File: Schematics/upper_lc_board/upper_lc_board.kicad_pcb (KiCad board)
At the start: 4 copper layers, 69.5 x 60 mm, 102 parts, among them J1 Stack Male Edge Connector, J3 PT, J4 TC, J5 SOL_CONN, J6 SOL2_CONN, Q1 MOSFET_BSS138, U1 ESP32-S3-WROOM-1-N16R2, U2 CAN_T_SN65HVD230DR, U3 PD_D3V3XA4B10LP, U4 ID_LM66100DCKR, U5 ID_LM66100DCKR, U6 TLV75801PDRV, U7 ADS131M04IPWR, U8 SSR_VO1400AEFTR, Y1 CRYSTAL_SIT8208AI

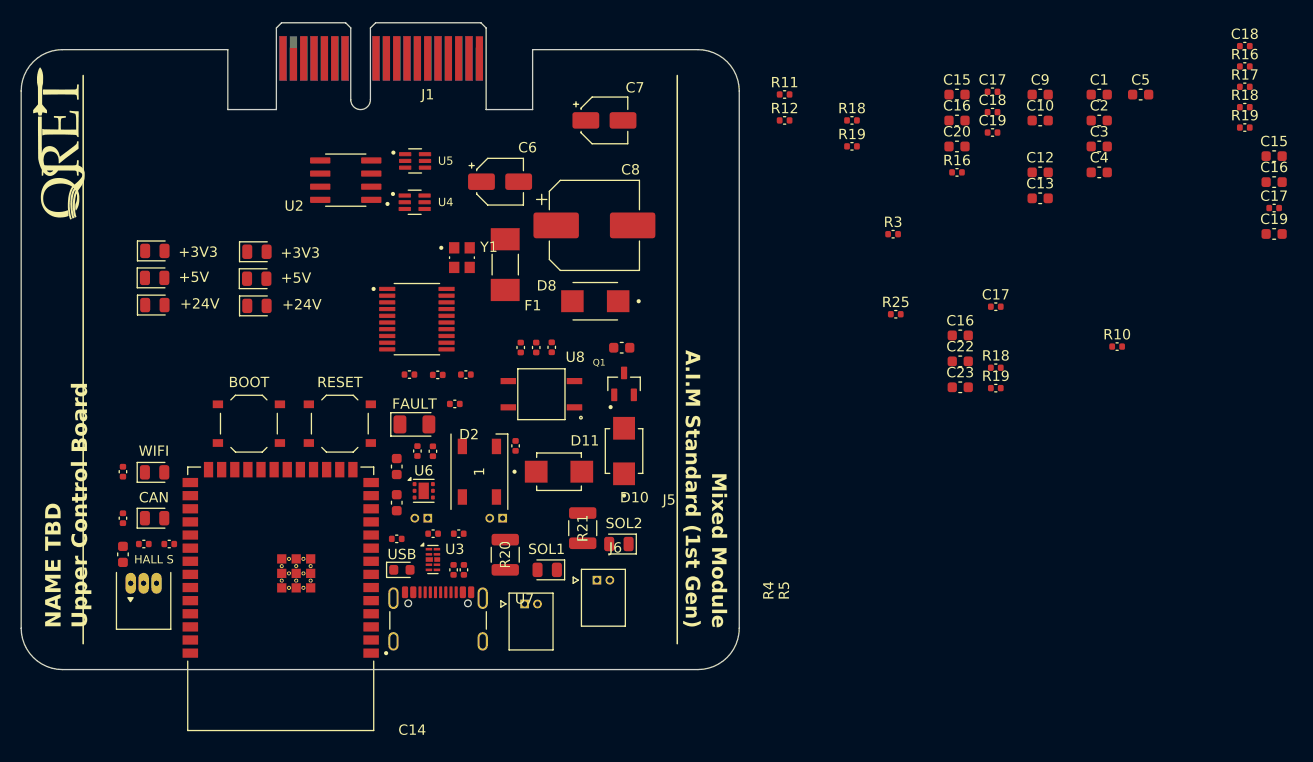
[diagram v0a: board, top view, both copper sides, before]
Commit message: update power circuitry (replaced OR-ing setup with a single power mux IC)
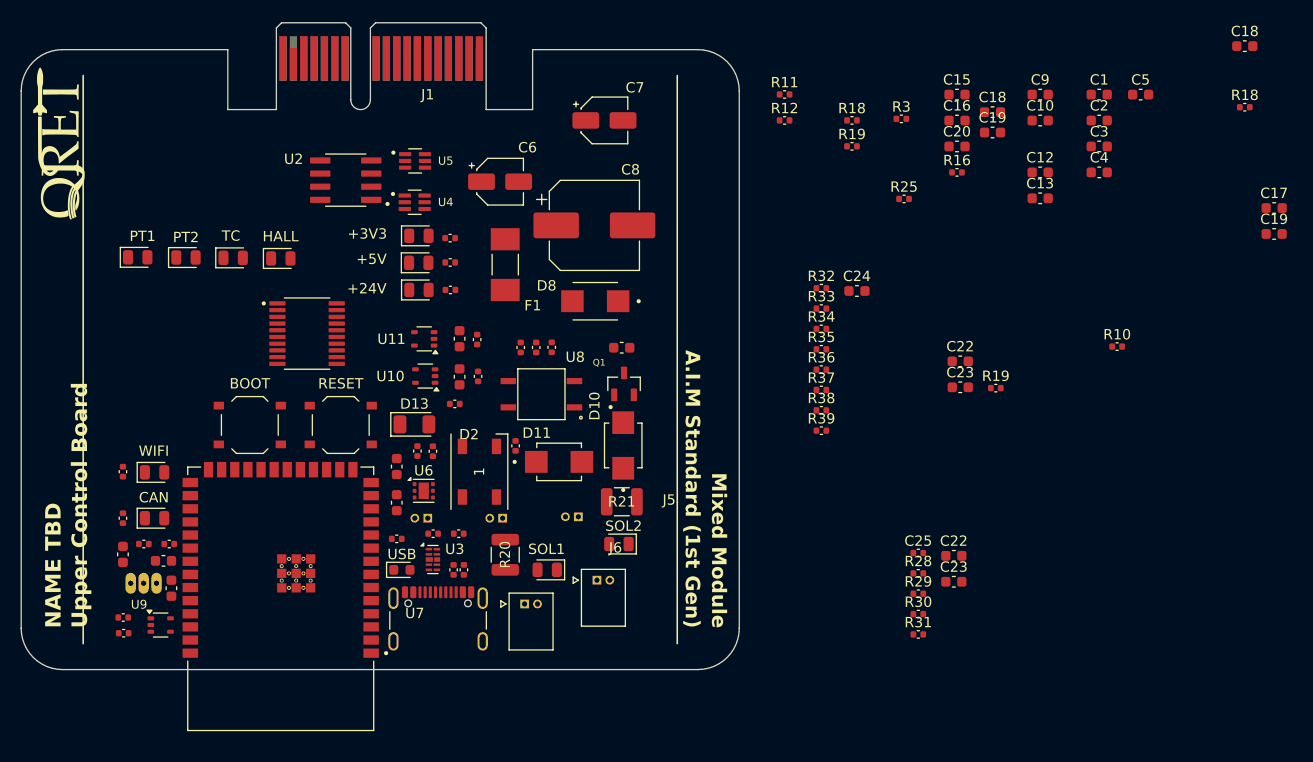
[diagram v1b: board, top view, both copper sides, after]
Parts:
- removed the C16 at (113.0, 47.8)
- removed the C17 at (116.5, 45.0)
- removed the D3 at (45.0, 39.7)
- removed the D4 at (44.9, 42.3)
- removed the D5 at (45.0, 45.0)
- removed Y1: CRYSTAL_SIT8208AI, SIT8208AI-G3-33E-65.000000T:OSC_SIT8208AI-G3-33E-65.000000T
- added C22: 1uF, Capacitor_SMD:C_0603_1608Metric, F.Cu at (112.4, 69.1)
- added C23: 1uF, Capacitor_SMD:C_0603_1608Metric, F.Cu at (112.4, 71.7)
- added C24: 10 nF, Capacitor_SMD:C_0603_1608Metric, F.Cu at (103.0, 43.5)
- added C25: 220 nF, Capacitor_SMD:C_0402_1005Metric, F.Cu at (109.0, 68.9)
- added C26: 0.1uF, Capacitor_SMD:C_0603_1608Metric, F.Cu at (64.6, 48.1)
- added D14: LED, LED_SMD:LED_0805_2012Metric, F.Cu at (33.4, 40.2)
- added D15: LED, LED_SMD:LED_0805_2012Metric, F.Cu at (38.1, 40.3)
- added D16: LED, LED_SMD:LED_0805_2012Metric, F.Cu at (42.7, 40.3)
- added D17: LED, LED_SMD:LED_0805_2012Metric, F.Cu at (47.3, 40.4)
- added J7: TC, 530480210:MOLEX_530480210, B.Cu at (76.1, 65.4)
- added R28: 330, Capacitor_SMD:C_0402_1005Metric, F.Cu at (109.0, 70.8)
- added R29: 330, Capacitor_SMD:C_0402_1005Metric, F.Cu at (109.0, 72.8)
- added R30: 330, Capacitor_SMD:C_0402_1005Metric, F.Cu at (109.0, 74.8)
- added R31: 330, Capacitor_SMD:C_0402_1005Metric, F.Cu at (109.0, 76.8)
- added R32: 1k, Capacitor_SMD:C_0402_1005Metric, F.Cu at (99.6, 43.2)
- added R33: 1k, Capacitor_SMD:C_0402_1005Metric, F.Cu at (99.6, 45.2)
- added R34: 1k, Capacitor_SMD:C_0402_1005Metric, F.Cu at (99.6, 47.2)
- added R35: 1k, Capacitor_SMD:C_0402_1005Metric, F.Cu at (99.6, 49.1)
- added R36: 1k, Capacitor_SMD:C_0402_1005Metric, F.Cu at (99.6, 51.1)
- added R37: 1k, Capacitor_SMD:C_0402_1005Metric, F.Cu at (99.6, 53.1)
- added R38: 1k, Capacitor_SMD:C_0402_1005Metric, F.Cu at (99.6, 55.1)
- added R39: 1k, Capacitor_SMD:C_0402_1005Metric, F.Cu at (99.6, 57.0)
- added U10: OA-TLV9001IDCK, Package_TO_SOT_SMD:SOT-353_SC-70-5, F.Cu at (61.3, 51.7)
- added U11: OA-TLV9001IDCK, Package_TO_SOT_SMD:SOT-353_SC-70-5, F.Cu at (61.2, 48.1)
- added U9: OA-TLV9001IDCK, Package_TO_SOT_SMD:SOT-353_SC-70-5, F.Cu at (35.6, 75.8)
- C17 (x2): value 220 nF -> 0.1uF; footprint Capacitor_SMD:C_0402_1005Metric -> Capacitor_SMD:C_0603_1608Metric
- C18: value 220 nF -> 10nF; footprint Capacitor_SMD:C_0402_1005Metric -> Capacitor_SMD:C_0603_1608Metric
- C18, C19: value 27 pF -> 10nF; footprint Capacitor_SMD:C_0402_1005Metric -> Capacitor_SMD:C_0603_1608Metric
- C19, C20: value 0.1uF -> 10nF
- HALL S: moved to B.Cu
- J3: value PT -> PT1
- J4: value TC -> PT2
- U2: value CAN_T_SN65HVD230DR -> CAN_TRX_SN65HVD230DR
- U7: value ADS131M04IPWR -> ADC_ADS131M04IPWR
- moved R16 120.9 mm to (32.0, 75.1)
- moved R17 120.7 mm to (32.1, 76.6)
- moved C15 114.6 mm to (36.7, 72.3), turned to 90 degrees
- moved C16 113.6 mm to (35.9, 69.6)
- moved R19 77.1 mm to (66.3, 48.2), turned to 90 degrees
- moved C17 58.5 mm to (64.6, 51.8), turned to 90 degrees
- moved R18 50.1 mm to (66.4, 51.8), turned to 90 degrees
- moved D3 25.6 mm to (60.6, 38.2)
- moved D4 25.6 mm to (60.6, 40.8)
- moved D5 25.6 mm to (60.6, 43.4)
- moved R10 13.3 mm to (63.7, 38.4), turned to 180 degrees
- moved R25 11.2 mm to (107.6, 34.6)
- moved R3 11.2 mm to (107.3, 26.9)
- moved R9 10.9 mm to (63.7, 40.8), turned to 180 degrees
- moved U7 10.7 mm to (49.8, 47.6)
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- renumbered FAULT to D13
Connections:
- C16 pad 1: GND -> +3V3 (x2)
- C16 pad 2: +3V3 -> GND (x2)
- C17 pad 1: Net-(U9-CAP) -> +3V3 (x2)
- C18 pad 1: Net-(U7-CAP) -> Net-(U7-AIN0N)
- C18 pad 2: GND -> Net-(U7-AIN0P)
- C18 pad 1: Net-(U7-XTAL1_CLKIN) -> Net-(U7-AIN0N)
- C18 pad 2: Net-(C18-Pad2) -> Net-(U7-AIN0P)
- C19 pad 1: Net-(U7-XTAL2) -> Net-(U7-AIN1N)
- C19 pad 2: Net-(C19-Pad2) -> Net-(U7-AIN1P)
- C19 pad 1: GND -> Net-(U7-AIN1N)
- C19 pad 2: +3V3 -> Net-(U7-AIN1P)
- C20 pad 1: GND -> Net-(U7-AIN2N)
- C20 pad 2: +3V3 -> Net-(U7-AIN2P)
- J3 pad 1: GND -> +24V
- J3 pad 2: +24V -> Net-(J3-Pin_2)
- J4 pad 1: GND -> +24V
- J4 pad 2: +24V -> Net-(J4-Pin_2)
- R6 pad 1: /ESP Breakout Cirucitry/GPIO_13 -> GPIO_13
- R7 pad 2: /ESP Breakout Cirucitry/GPIO_13 -> GPIO_13
- U1 pad 11: /ESP Breakout Cirucitry/GPIO_18 -> GPIO_18
- U1 pad 13: unconnected-(U1-IO19-Pad13) -> GPIO_18
- U1 pad 21: unconnected-(U1-IO13-Pad21) -> GPIO_13
- U1 pad 22: unconnected-(U1-IO14-Pad22) -> GPIO_14
- U1 pad 8: unconnected-(U1-IO15-Pad8) -> GPIO_15
- U1 pad 9: unconnected-(U1-IO16-Pad9) -> GPIO_16
- U2 pad 4: /ESP Breakout Cirucitry/GPIO_18 -> GPIO_18
- U7 pad 10: unconnected-(U7-AIN3P-Pad10) -> Net-(U7-AIN3P)
- U7 pad 11: GPIO_8 -> +3V3
- U7 pad 12: GPIO_7 -> GND
- U7 pad 16: unconnected-(U7-DIN-Pad16) -> GPIO_16
- U7 pad 17: Net-(U7-CLKIN) -> GPIO_18
- U7 pad 4: GND -> Net-(U7-AIN0N)
- U7 pad 5: GND -> Net-(U7-AIN1N)
- U7 pad 7: /Sensor Circuitry/HALL_OUT -> Net-(U7-AIN2P)
- U7 pad 8: GND -> Net-(U7-AIN2N)
- U7 pad 9: unconnected-(U7-AIN3N-Pad9) -> Net-(U7-AIN3N)
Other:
- board text added: "HALL"
- board text added: "PT1"
- board text added: "PT2"
- board text added: "TC"
- board text removed: "0.1mm grid used."
- board text removed: "D_TVS"

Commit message: reviewing schematics
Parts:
- removed the R10 at (128.2, 48.9)
- removed U5: ID_LM66100DCKR, LM66100DCKR:SOT65P210X110-6N
- R13: value 1.12M -> 100k
- R14: value 200k -> 20k
- R23: value 340 -> 180
- U4: value ID_LM66100DCKR -> PMUX_TPS2121RUXR; footprint LM66100DCKR:SOT65P210X110-6N -> TPS2121RUXR:IC_TPS2121RUXR
- moved U4 1.95 mm to (60.0, 33.0)
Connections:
- R20 pad 1: Net-(D7-A) -> Net-(D7-K)
- R21 pad 1: Net-(D9-A) -> Net-(D9-K)
- U4 pad 1: /Power Circuitry/3V3_BP -> +3V3
- U4 pad 2: GND -> /Power Circuitry/3V3_USB
- U4 pad 3: Net-(U4-~{CE}) -> GND
- U4 pad 4: unconnected-(U4-NC-Pad4) -> GND
- U4 pad 6: +3V3 -> /Power Circuitry/3V3_USB

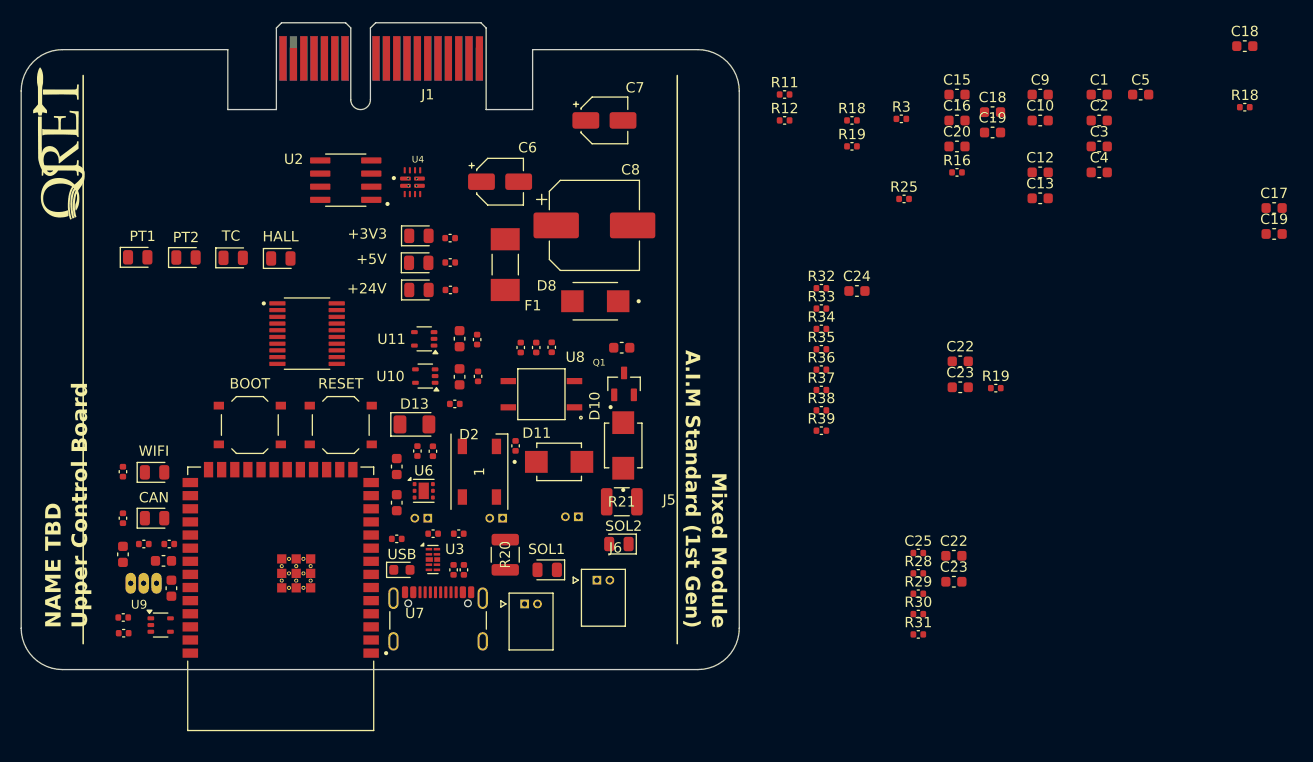
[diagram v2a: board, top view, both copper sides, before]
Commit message: finish power circuitry (MUX)
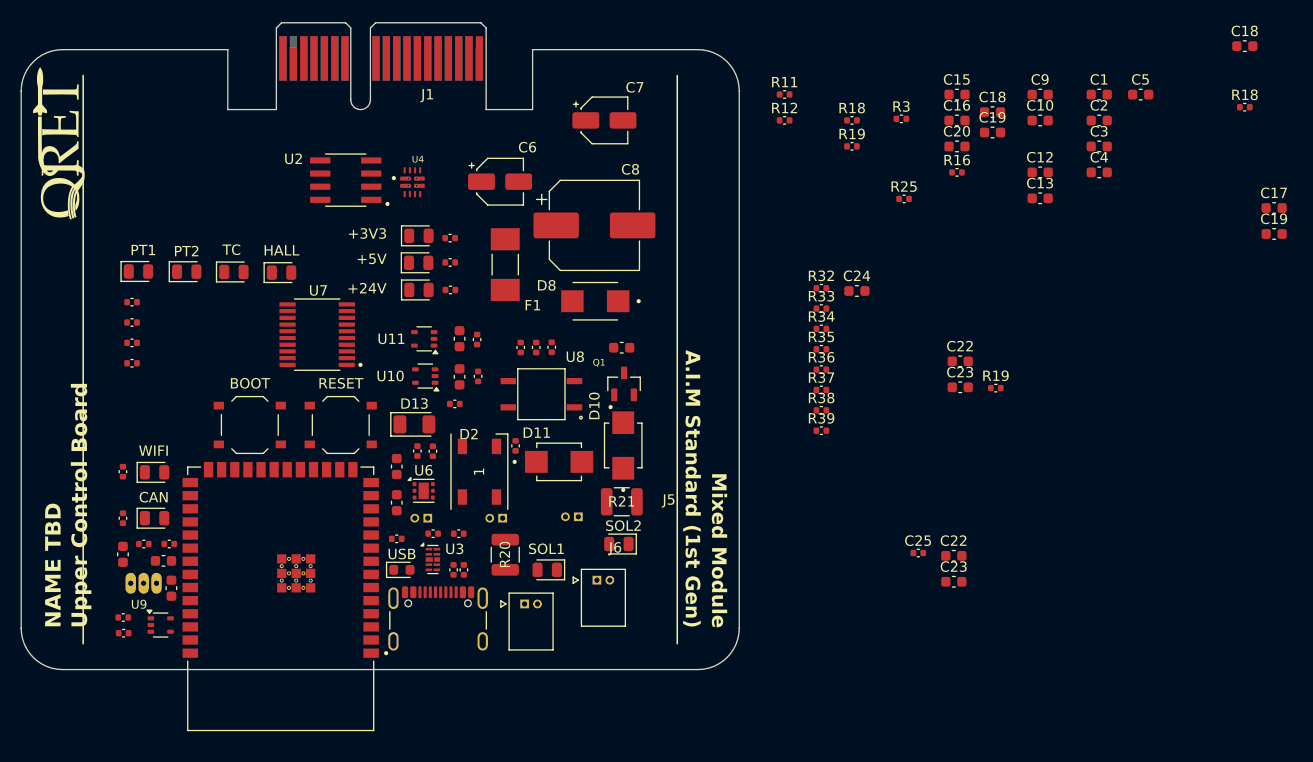
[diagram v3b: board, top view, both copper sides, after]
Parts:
- moved R28 80.5 mm to (32.9, 44.6)
- moved R29 80.5 mm to (32.9, 46.6)
- moved R30 80.5 mm to (32.9, 48.5)
- moved R31 80.5 mm to (32.9, 50.5)
- moved D16 1.37 mm to (42.7, 41.7)
- moved D14 1.37 mm to (33.5, 41.6)
- moved D15 1.37 mm to (38.2, 41.6)
- moved D17 1.37 mm to (47.4, 41.7)
- moved U7 0.99 mm to (50.8, 47.7), turned to 180 degrees

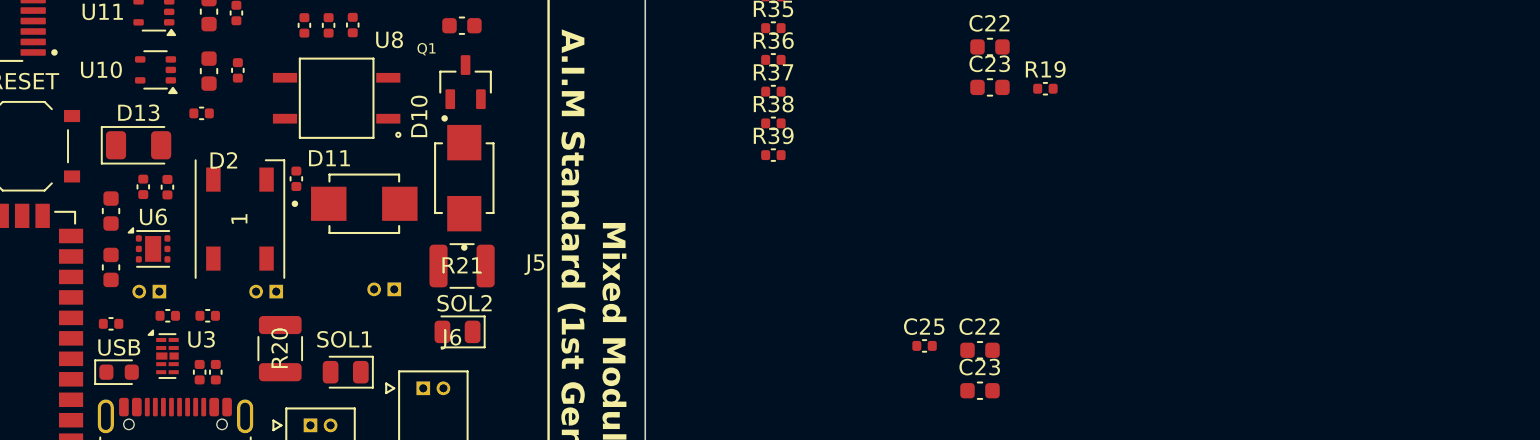
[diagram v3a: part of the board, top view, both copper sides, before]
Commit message: add TC circuitry; finish layout next.
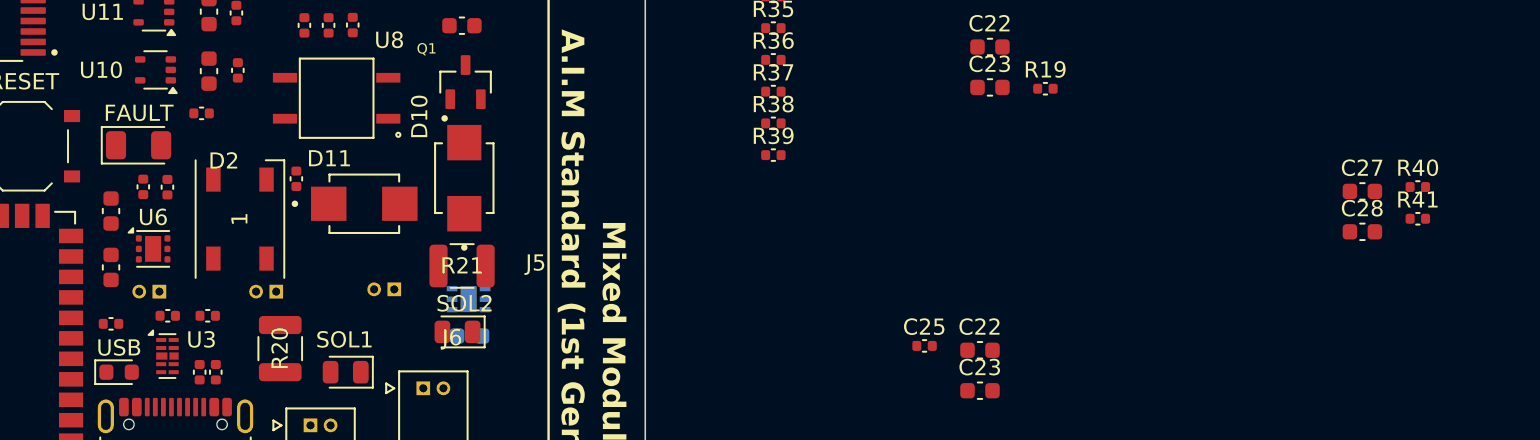
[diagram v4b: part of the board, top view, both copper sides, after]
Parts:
- added C27: 0.1uF, Capacitor_SMD:C_0603_1608Metric, F.Cu at (136.2, 59.3)
- added C28: 10nF, Capacitor_SMD:C_0603_1608Metric, F.Cu at (136.2, 61.8)
- added C29: 0.1uF, Capacitor_SMD:C_0603_1608Metric, B.Cu at (80.7, 68.3)
- added R40: 60, Capacitor_SMD:C_0402_1005Metric, F.Cu at (139.6, 59.0)
- added R41: 60, Capacitor_SMD:C_0402_1005Metric, F.Cu at (139.6, 61.0)
- added U5: TMP117MAIDRVR, TMP117MAIDRVR:SON65P200X200X80-7N, B.Cu at (80.7, 66.0)
- renumbered D13 to FAULT
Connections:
- R1 pad 1: /ESP Breakout Cirucitry/GPIO_5 -> /ESP Breakout Cirucitry/GPIO_6
- R20 pad 1: Net-(D7-K) -> Net-(D7-A)
- R21 pad 1: Net-(D9-K) -> Net-(D9-A)
- R6 pad 1: GPIO_13 -> /ESP Breakout Cirucitry/GPIO_21
- R7 pad 2: GPIO_13 -> /ESP Breakout Cirucitry/GPIO_21
- U1 pad 11: GPIO_18 -> /ESP Breakout Cirucitry/GPIO_18
- U1 pad 13: GPIO_18 -> /ESP Breakout Cirucitry/USB_N
- U1 pad 14: unconnected-(U1-IO20-Pad14) -> /ESP Breakout Cirucitry/USB_P
- U1 pad 15: unconnected-(U1-IO3-Pad15) -> /ESP Breakout Cirucitry/GPIO_3
- U1 pad 16: unconnected-(U1-IO46-Pad16) -> /ESP Breakout Cirucitry/GPIO_46
- U1 pad 20: GPIO_11 -> GPIO_12
- U1 pad 23: unconnected-(U1-IO21-Pad23) -> /ESP Breakout Cirucitry/GPIO_21
- U1 pad 24: unconnected-(U1-IO47-Pad24) -> /ESP Breakout Cirucitry/GPIO_47
- U1 pad 25: unconnected-(U1-IO48-Pad25) -> GPIO_48
- U1 pad 26: unconnected-(U1-IO45-Pad26) -> /ESP Breakout Cirucitry/GPIO_45
- U1 pad 28: unconnected-(U1-IO35-Pad28) -> /ESP Breakout Cirucitry/GPIO_35
- U1 pad 29: unconnected-(U1-IO36-Pad29) -> /ESP Breakout Cirucitry/GPIO_36
- U1 pad 30: unconnected-(U1-IO37-Pad30) -> /ESP Breakout Cirucitry/GPIO_37
- U1 pad 31: unconnected-(U1-IO38-Pad31) -> GPIO_38
- U1 pad 32: unconnected-(U1-IO39-Pad32) -> /ESP Breakout Cirucitry/GPIO_39
- U1 pad 33: unconnected-(U1-IO40-Pad33) -> /ESP Breakout Cirucitry/GPIO_40
- U1 pad 34: unconnected-(U1-IO41-Pad34) -> /ESP Breakout Cirucitry/GPIO_41
- U1 pad 35: unconnected-(U1-IO42-Pad35) -> /ESP Breakout Cirucitry/GPIO_42
- U1 pad 36: unconnected-(U1-RXD0-Pad36) -> /ESP Breakout Cirucitry/RX_DO
- U1 pad 37: unconnected-(U1-TXD0-Pad37) -> /ESP Breakout Cirucitry/TX_DO
- U1 pad 38: unconnected-(U1-IO2-Pad38) -> /ESP Breakout Cirucitry/GPIO_2
- U1 pad 39: unconnected-(U1-IO1-Pad39) -> /ESP Breakout Cirucitry/GPIO_1
- U1 pad 6: GPIO_6 -> /ESP Breakout Cirucitry/GPIO_6
- U2 pad 4: GPIO_18 -> /ESP Breakout Cirucitry/GPIO_18
- U2 pad 5: unconnected-(U2-VREF-Pad5) -> Net-(U2-VREF)
- U4 pad 2: /Power Circuitry/3V3_USB -> /Power Circuitry/3V3_BP
- U4 pad 2_1: /Power Circuitry/3V3_USB -> /Power Circuitry/3V3_BP
- U4 pad 3: GND -> Net-(U4-CP2)
- U4 pad 7: /Power Circuitry/3V3_BP -> /Power Circuitry/3V3_USB
- U4 pad 7_1: /Power Circuitry/3V3_BP -> /Power Circuitry/3V3_USB
- U7 pad 13: GPIO_6 -> GPIO_10
- U7 pad 17: GPIO_18 -> GPIO_48
